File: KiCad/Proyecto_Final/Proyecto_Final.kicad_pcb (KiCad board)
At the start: 4 copper layers, 100 x 100 mm, 216 parts, among them IC1 SKY13335-381LF, IC2 SKY13335-381LF, IC3 SKY13335-381LF, IC4 SKY13335-381LF, IC5 SKY13335-381LF, IC6 SKY13335-381LF, J1 TP_I, J10 PB, J11 PE, J12 PC, J13 SPI4, J14 CLK_OUT0, J15 OutEn, J16 ClkSel, J17 CLK_IN, J18 RF_IN, J2 TP_Q, J3 I2C1, J4 Power, J5 ARM SWD, J6 Conn_USB, J7 Boot_Select, J8 PA, J9 PD, Q1 Si2301CDS, SW1 Reset, T1 2450BL05A0100, T2 B0310J50100AHF, T3 B0310J50100AHF, U1 MAX1193ETI+, U2 MAX2837, U3 AMS1117-3.3, U4 USBLC6-2SC6, U5 STM32F723ZCTx, U6 5P49V5929, U7 RFFC5072, U8 MAAL-010200, Y1 25MHz

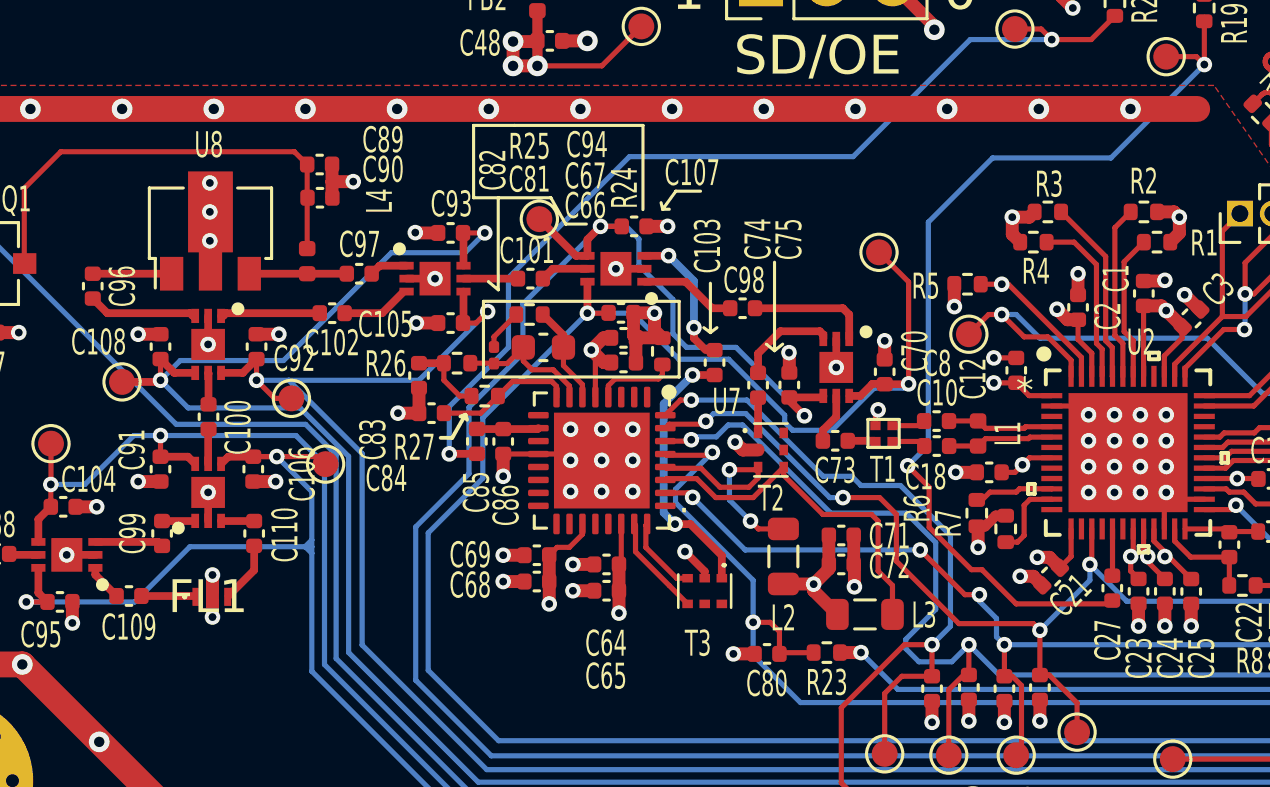
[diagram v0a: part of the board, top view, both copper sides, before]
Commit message: Cambiado balun del transceptor.
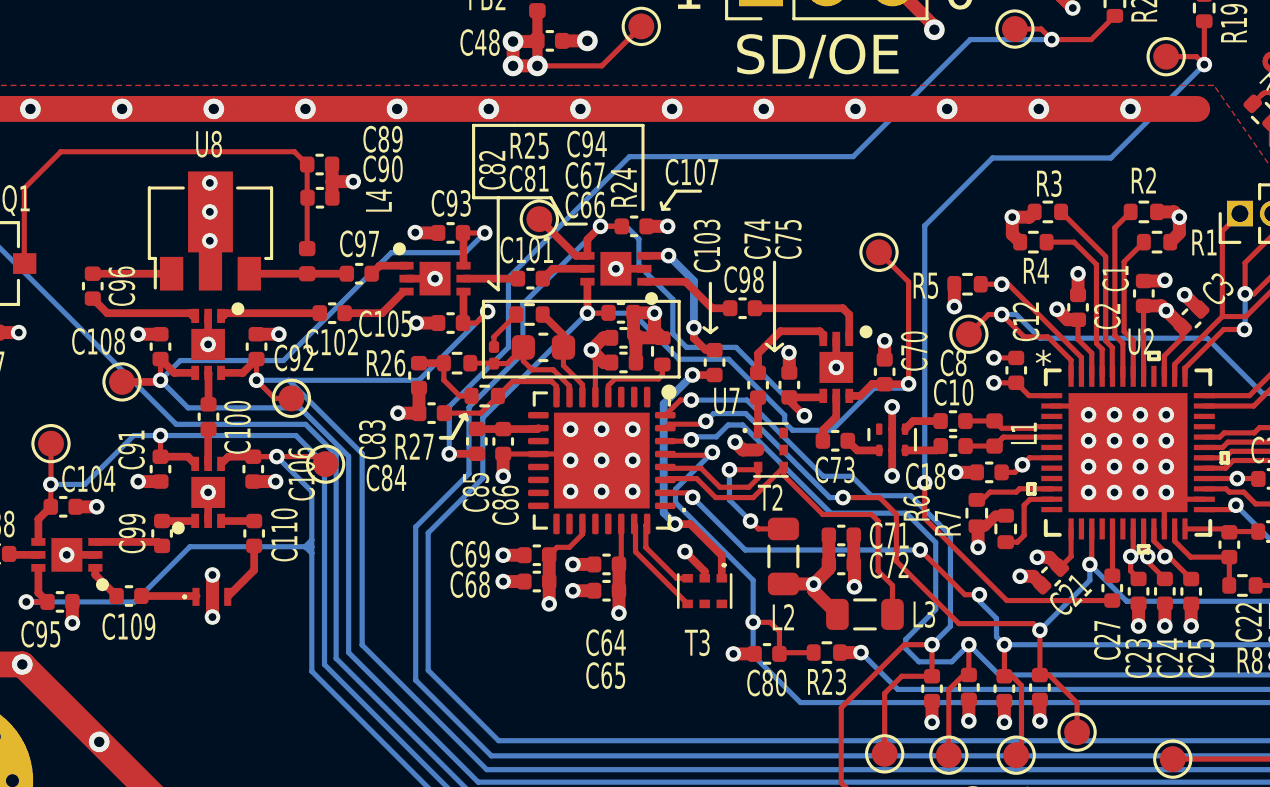
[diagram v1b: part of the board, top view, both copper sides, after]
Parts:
- T1: value 2450BL05A0100 -> 2500BL14M100; footprint Tesis2020-21:0202_Balun -> RF_Converter:Balun_Johanson_1.6x0.8mm
- moved T1 0.68 mm to (110.9, 132.3), turned to 90 degrees
- moved C10 0.64 mm to (113.2, 132.6)
- moved C8 0.64 mm to (113.2, 131.6)
- moved L1 0.64 mm to (114.8, 132.1)
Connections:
- T1 pad 1: GND -> RF_IF
- T1 pad 2: RF_IF -> GND
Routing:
- net GND: track 221.0 -> 223.1 mm, vias 199 -> 200
- net Trx_CLK: track 37.3 -> 36.6 mm
- net /Transceptor/RXRF+: track 4.11 -> 3.47 mm
- net /Transceptor/RXRF-: track 4.11 -> 3.47 mm

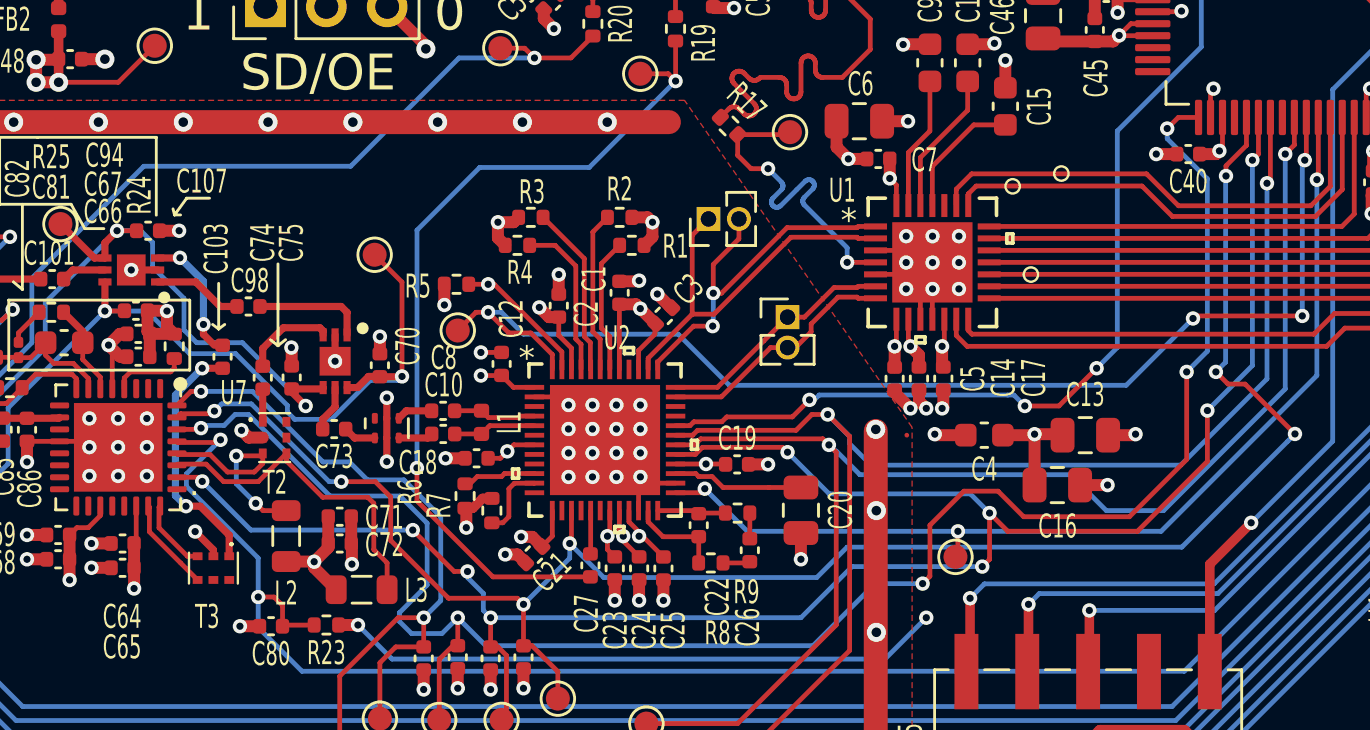
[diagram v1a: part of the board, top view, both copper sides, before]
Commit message: Removidos archivos innecesarios y revisión de placa.
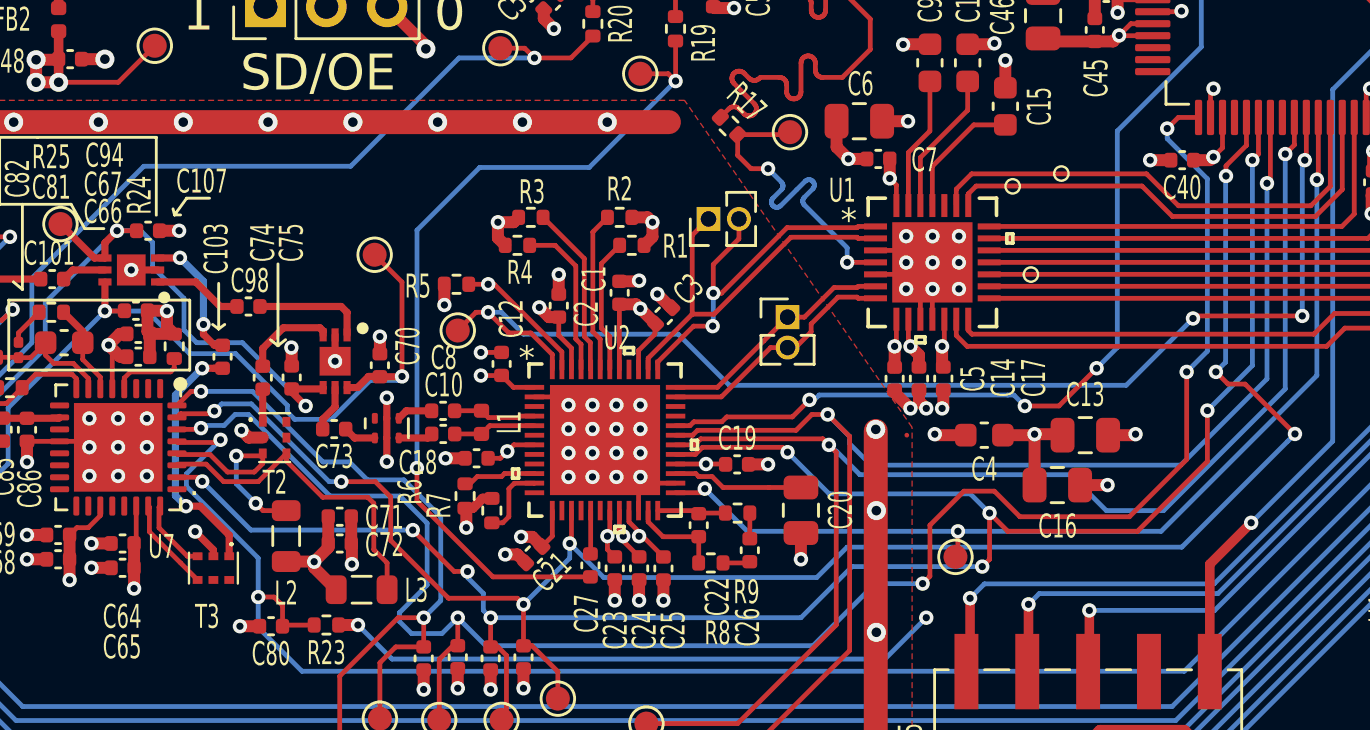
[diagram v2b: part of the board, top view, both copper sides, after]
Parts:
- moved C40 0.36 mm to (144.1, 121.1)

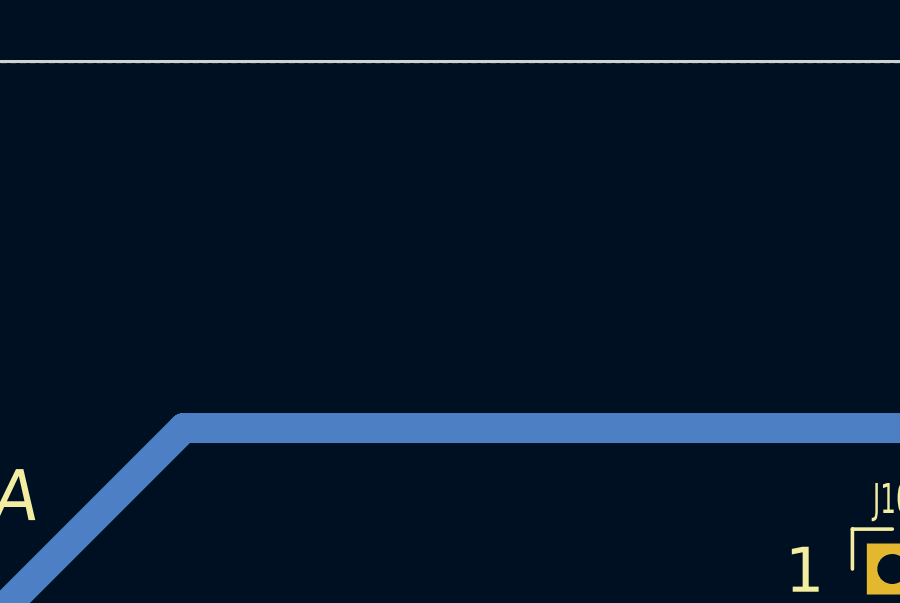
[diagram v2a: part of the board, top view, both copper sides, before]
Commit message: agregado logo gintea.
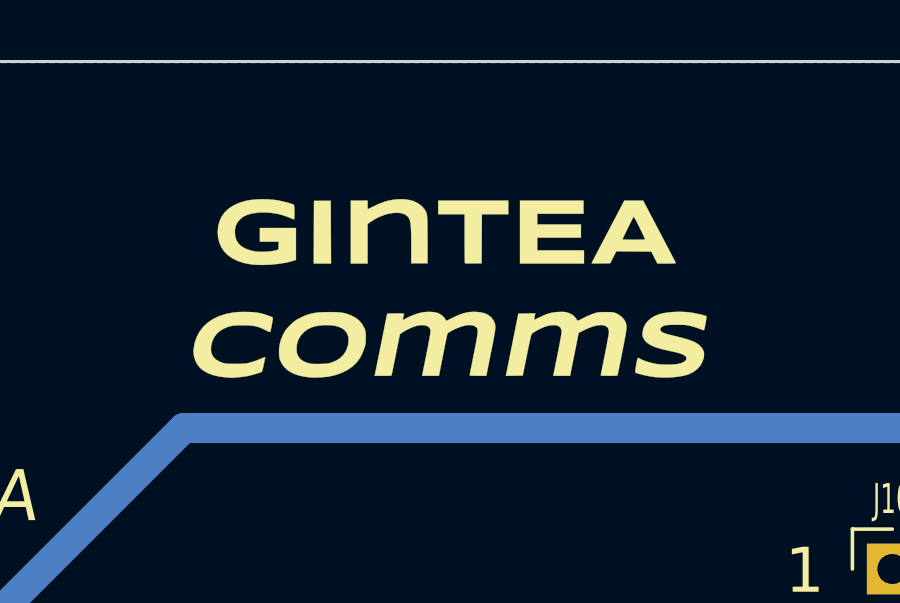
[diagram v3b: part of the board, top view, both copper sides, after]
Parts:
- added G***: LOGO, Tesis2020-21:logo_gintea_comms, F.Cu at (129.2, 57.5)

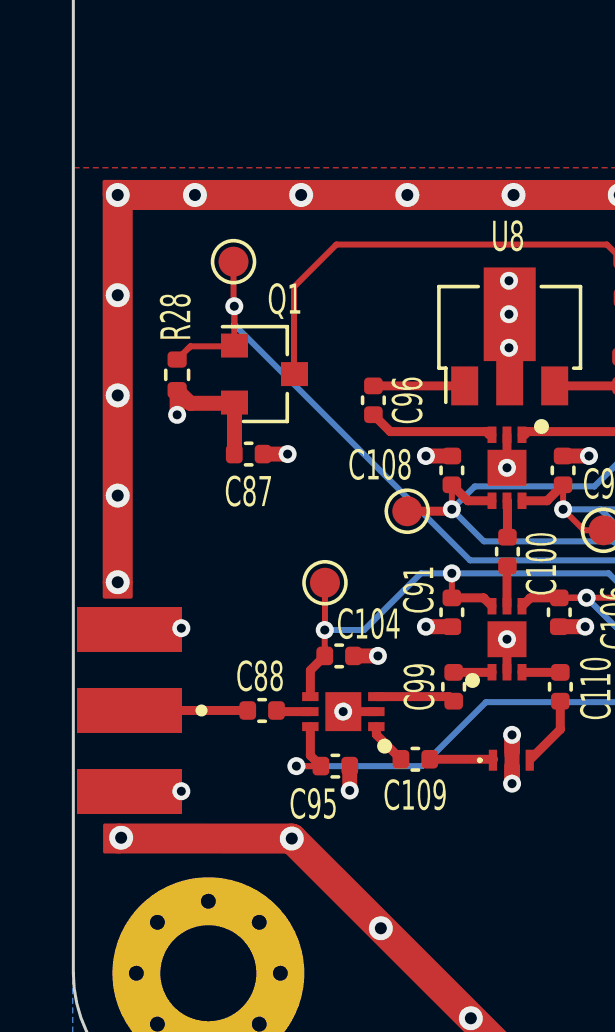
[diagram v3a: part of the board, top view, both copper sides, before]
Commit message: ajustado conector sma de entrada.
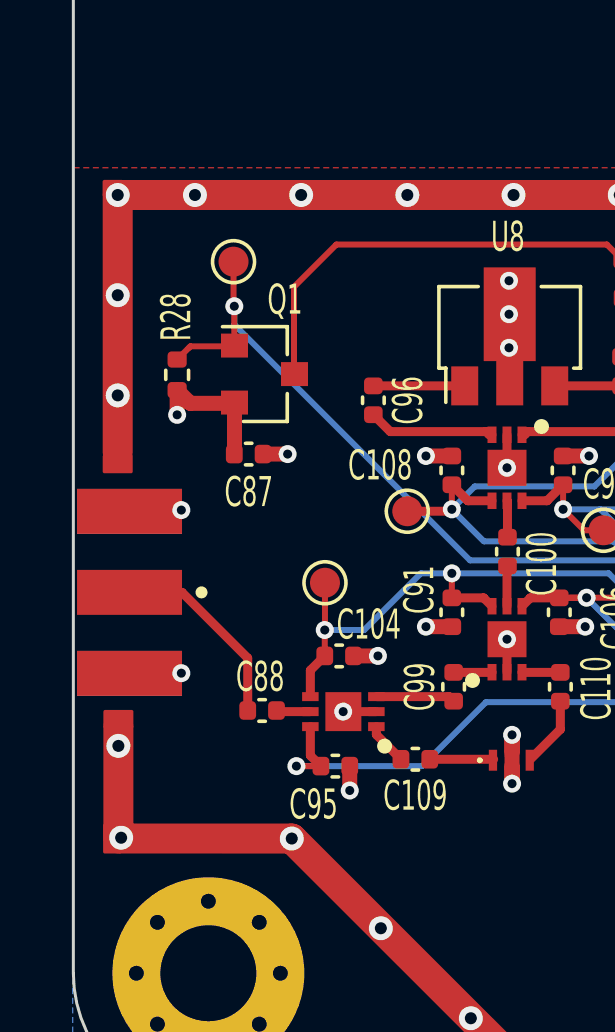
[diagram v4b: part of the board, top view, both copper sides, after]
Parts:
- moved J18 3.94 mm to (71.9, 132.8)
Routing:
- net Net-(C88-Pad2): track 3.94 -> 6.59 mm
- net GND: vias 200 -> 199

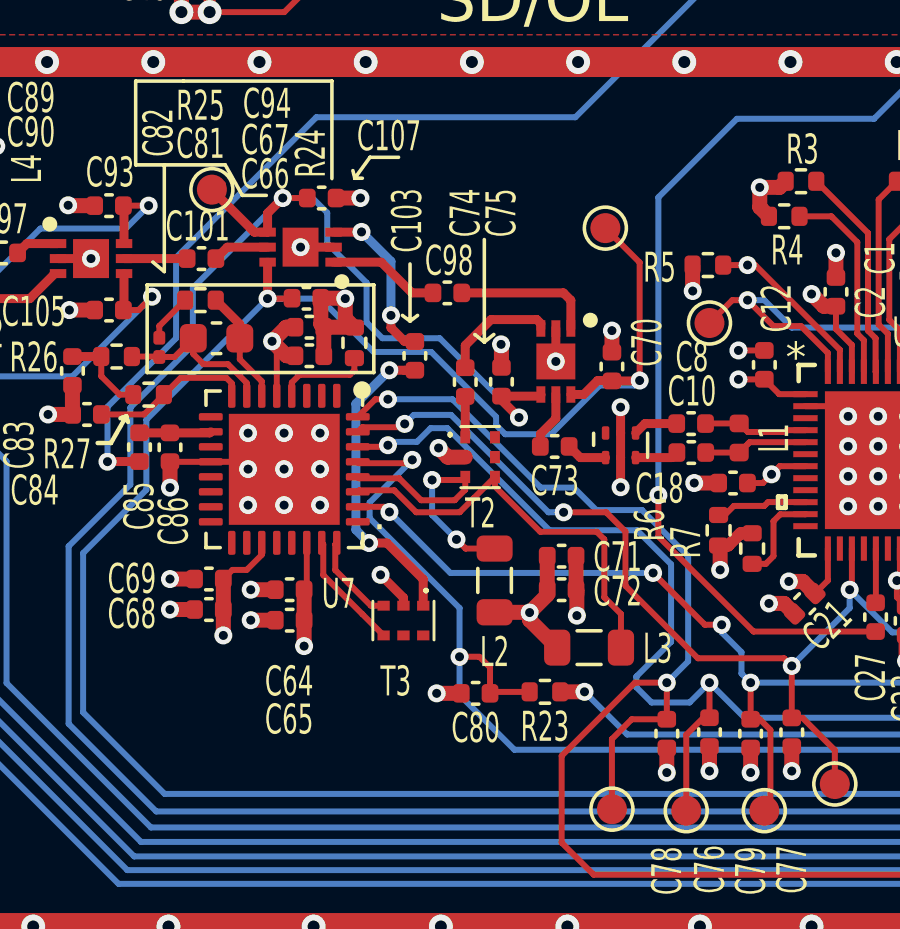
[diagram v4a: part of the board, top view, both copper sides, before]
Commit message: Agregados capacitores de balunes faltantes
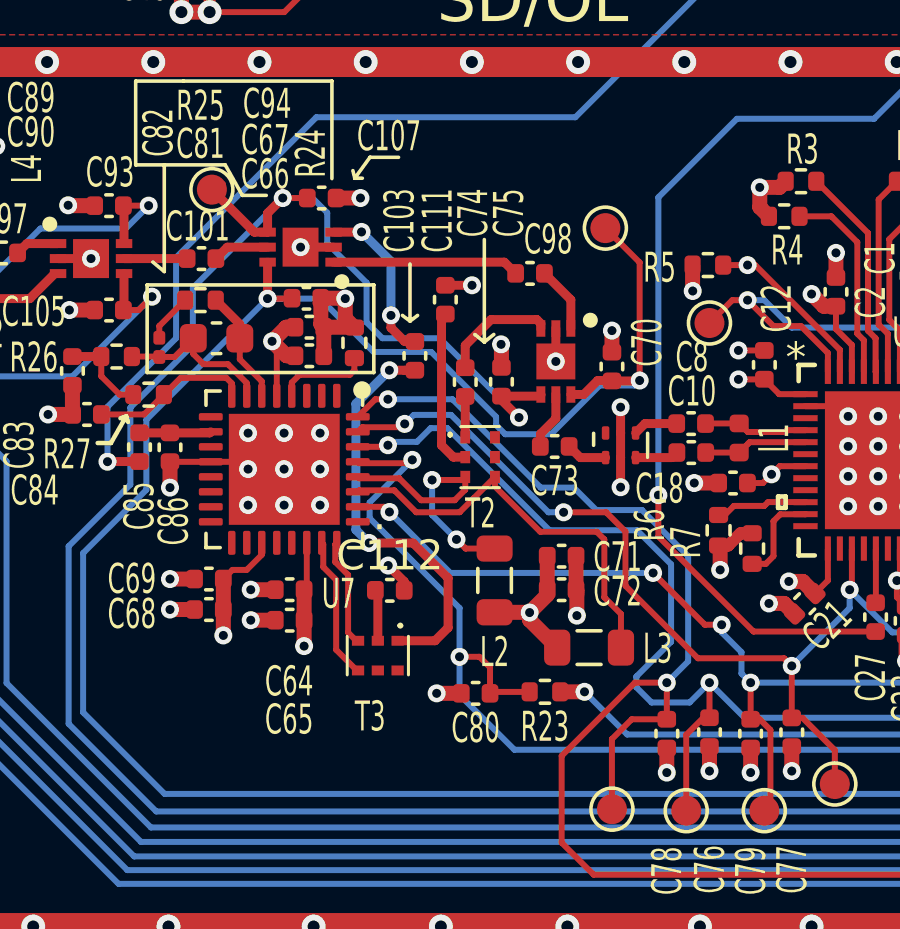
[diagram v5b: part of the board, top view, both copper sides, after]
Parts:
- added C111: 100nF, Capacitor_SMD:C_0402_1005Metric, F.Cu at (105.0, 127.5)
- added C112: 100nF, Capacitor_SMD:C_0402_1005Metric, F.Cu at (103.2, 137.2)
- moved C98 2.83 mm to (107.9, 126.6)
- moved T3 1.45 mm to (102.8, 139.3)
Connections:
- T2 pad 2: GND -> Net-(C111-Pad1)
- T3 pad 2: GND -> Net-(C112-Pad1)
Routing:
- net Net-(C111-Pad1): track 0.00 -> 5.38 mm
- net Net-(C103-Pad1): track 10.4 -> 13.9 mm
- net Net-(C98-Pad2): track 3.74 -> 6.22 mm
- net SWITCH: track 4.68 -> 2.20 mm
- net Net-(C112-Pad1): track 0.00 -> 1.72 mm
- net MIX_IPP: track 3.94 -> 4.78 mm
- net MIX_IPN: track 3.03 -> 3.63 mm
